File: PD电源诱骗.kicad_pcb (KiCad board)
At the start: 2 copper layers, 74.2 x 61 mm, 33 parts, among them J1 USB_C_Receptacle_USB2.0_16P, J2 电源IO, U1 TPS5430DDA, U2 CH224A, U3 XL6019

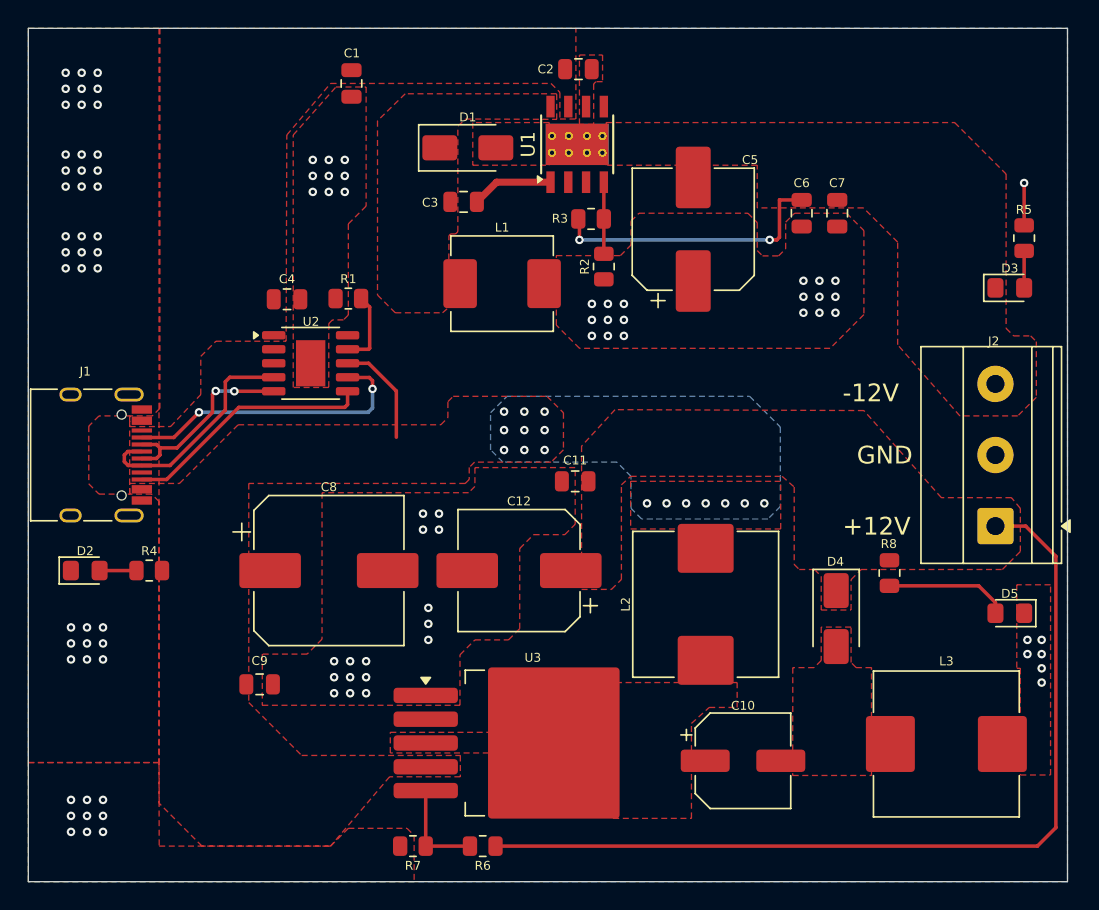
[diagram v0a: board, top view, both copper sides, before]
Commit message: 修改为诱骗9V+BOOST得到12V
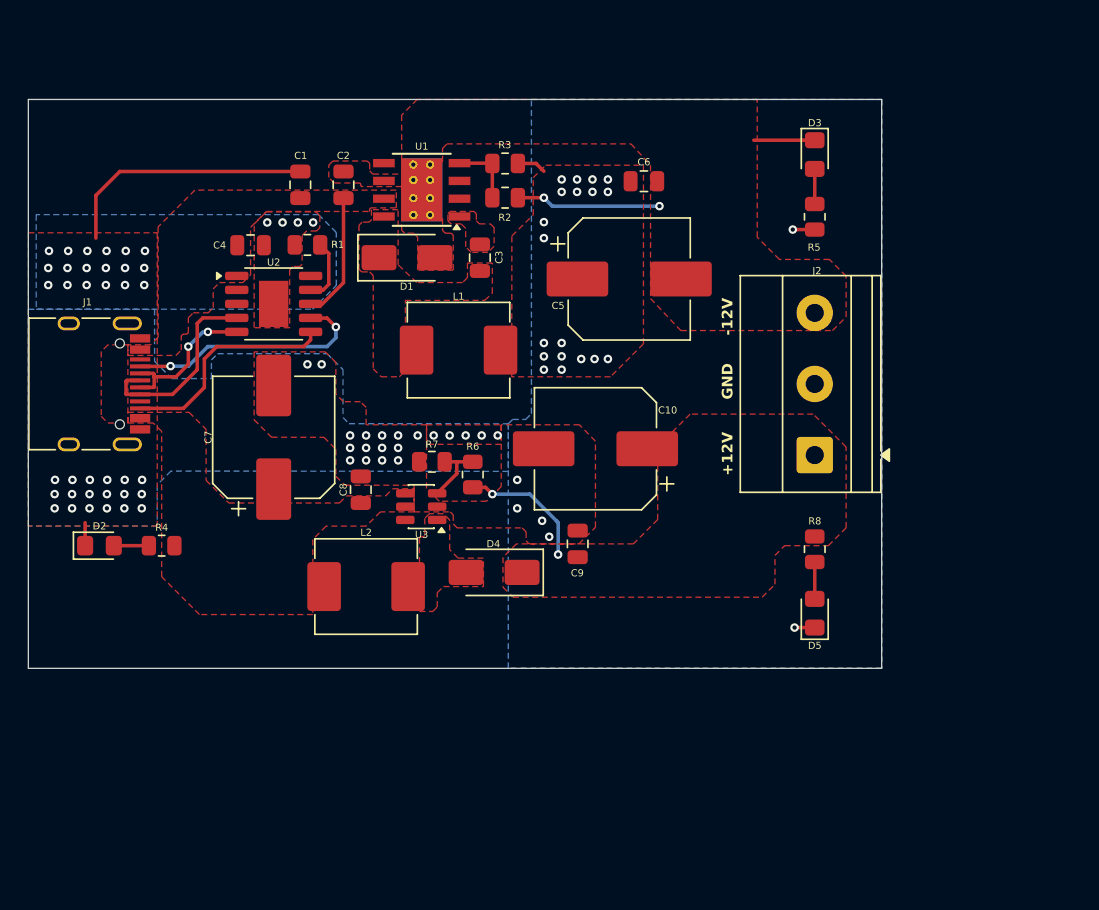
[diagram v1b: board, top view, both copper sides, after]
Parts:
- removed C11: 1uF, Capacitor_SMD:C_0805_2012Metric
- removed C12: 220uF/25V, Capacitor_SMD:CP_Elec_8x10.5
- removed L3: 47uH/5A, Inductor_SMD:L_Wuerth_HCI-1040
- C10: value 22uF/63V -> 220uF/25V; footprint Capacitor_SMD:CP_Elec_6.3x7.7 -> Capacitor_SMD:CP_Elec_8x10.5
- C7: value 1nF -> 220uF/25V; footprint Capacitor_SMD:C_0805_2012Metric -> Capacitor_SMD:CP_Elec_8x10.5
- C8: value 220uF/50V -> 1uF; footprint Capacitor_SMD:CP_Elec_10x10.5 -> Capacitor_SMD:C_0805_2012Metric
- D2: value LED -> LED RED
- D3: value LED -> LED BLUE
- D5: value LED -> LED GREEN
- L1: value 33uH -> 22uH
- L2: value 47uH/5A -> 22uH; footprint Inductor_SMD:L_Wuerth_HCI-1040 -> Inductor_SMD:L_TechFuse_SL0630
- R1: value 56K -> 6.8K
- R5, R8: value 3K -> 5K
- R6: value 24K -> 39K
- R7: value 2.7K -> 2K
- U3: value XL6019 -> MT3608; footprint Package_TO_SOT_SMD:TO-263-5_TabPin3 -> Package_TO_SOT_SMD:SOT-23-6
- moved C7 43.3 mm to (105.9, 113.5), turned to 90 degrees
- moved R7 27.5 mm to (117.2, 115.3)
- moved R6 26.6 mm to (120.1, 116.2), turned to 90 degrees
- moved C9 24.8 mm to (127.6, 121.2), turned to 90 degrees
- moved C10 24.7 mm to (128.9, 114.4), turned to 180 degrees
- moved D4 24.7 mm to (121.7, 123.2), turned to 180 degrees
- moved L2 24.3 mm to (112.5, 124.2), turned to 0 degrees
- moved C2 18.7 mm to (110.9, 95.5), turned to 90 degrees
- moved U3 18.7 mm to (116.5, 118.5), turned to 180 degrees
- moved D3 16.9 mm to (144.6, 93.3), turned to -90 degrees
- moved R5 15.0 mm to (144.6, 97.8), turned to 90 degrees
- moved D5 13.9 mm to (144.6, 126.1), turned to 90 degrees
- moved J2 13.9 mm to (144.6, 114.8)
- moved U1 11.6 mm to (116.5, 95.9), turned to 180 degrees
- moved C6 11.5 mm to (132.4, 95.2), turned to 180 degrees
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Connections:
- C10 pad 1: Net-(U3-SW) -> +12V
- C10 pad 2: Net-(D4-A) -> GND
- C7 pad 1: -12V -> VCC
- C9 pad 1: VCC -> +12V
- L2 pad 2: Net-(U3-SW) -> Net-(D4-A)
- U3 pad 1: GND -> Net-(D4-A)
- U3 pad 2: unconnected-(U3-EN-Pad2) -> GND
- U3 pad 3: Net-(U3-SW) -> Net-(U3-FB)
- U3 pad 5: Net-(U3-FB) -> VCC
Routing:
- net +12V: track 65.2 -> 9.42 mm, vias 0 -> 2
- net GND: track 3.03 -> 25.1 mm, vias 95 -> 85
- net Net-(D5-A): track 8.83 -> 2.63 mm
- net Net-(U1-BOOT): track 5.84 -> 0.00 mm
- net -12V: track 20.1 -> 14.7 mm
- net Net-(J1-CC1): track 21.2 -> 17.7 mm
- net Net-(U2-DM): track 13.9 -> 10.9 mm
- net Net-(U2-DP): track 16.4 -> 14.1 mm
- net Net-(U3-FB): track 7.13 -> 4.84 mm
- net Net-(J1-CC2): track 17.9 -> 16.0 mm
- net VCC: track 7.61 -> 9.02 mm, vias 16 -> 0
- net /R_REF: track 5.42 -> 4.53 mm
- added copper zone on F.Cu, net Net-(U1-BOOT)
- removed copper zone on F.Cu, net Net-(U3-SW)
- removed copper zone on B.Cu, net VCC
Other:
- board size 74.2 x 61 mm -> 61 x 40.6 mm

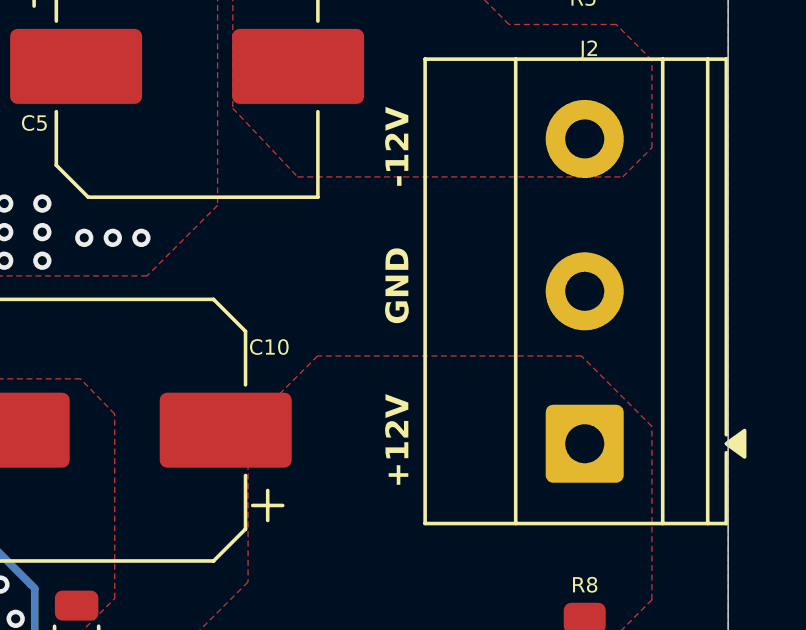
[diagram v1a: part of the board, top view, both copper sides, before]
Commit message: V2，更改诱骗电压为+9V
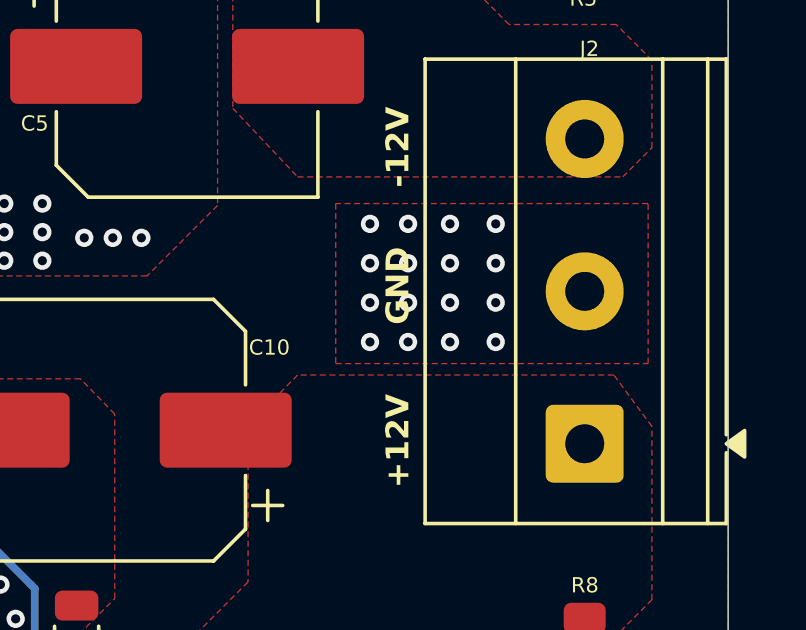
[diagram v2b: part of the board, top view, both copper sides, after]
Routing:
- net GND: vias 85 -> 101
